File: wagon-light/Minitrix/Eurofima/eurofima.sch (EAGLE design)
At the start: 55 parts, among them IC2 78L05F, IC3 16F18324-SL, Q1 BC817-25SMD, Q2 BC817-16SMD, Q3 BC817-16SMD, Q4 BC817-16SMD, Q5 BC817-16SMD, Q6 BC817-16SMD, Q7 BC817-16SMD, Q8 BC817-16SMD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

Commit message: roco eurofima
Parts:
- removed LED17, LED18: (no value), led:LED3MM
- removed R10, R5, R6, R9: (no value), rcl:R-EU_R1206
- added Q10, Q11, Q12, Q13: BC817-16SMD, transistor-npn:BC817-16SMD
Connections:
- removed net N$8: LED5.A, R6.1
- removed net N$9: LED1.A, R3.1
- removed net PWM7: Q4.B, Q5.C
- removed net PWM8: Q6.B, Q7.C
- removed net PWM9: Q8.B, Q9.C
- net +15V: now also LED1.A, LED13.A, LED5.A, LED9.A; no longer LED18.A, R3.2, R4.2, R5.2, R6.2
- net GND: now also Q11.E, Q13.E, R3.1, R4.1
- net N$27: now also Q10.C; no longer LED17.C, R9.2
- net N$29: now also Q12.C; no longer LED18.C, R10.2
- net N$6: now also Q10.E, Q11.B, R3.2; no longer LED13.A, R5.1
- net N$7: now also Q12.E, Q13.B, R4.2; no longer LED9.A, R4.1
- net PWM1: now also Q8.B, Q9.C
- net PWM2: now also Q4.B, Q5.C
- net PWM3: now also Q6.B, Q7.C; no longer Q2.B, Q3.C
- net PWM4: now also Q2.B, Q3.C
- net PWM5: now also Q10.B, Q11.C
- net PWM6: now also Q12.B, Q13.C
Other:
- moved on the sheet: LED10, LED11, LED12, LED13, LED14, LED15, LED16, LED9, Q2, Q3, Q6, Q7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

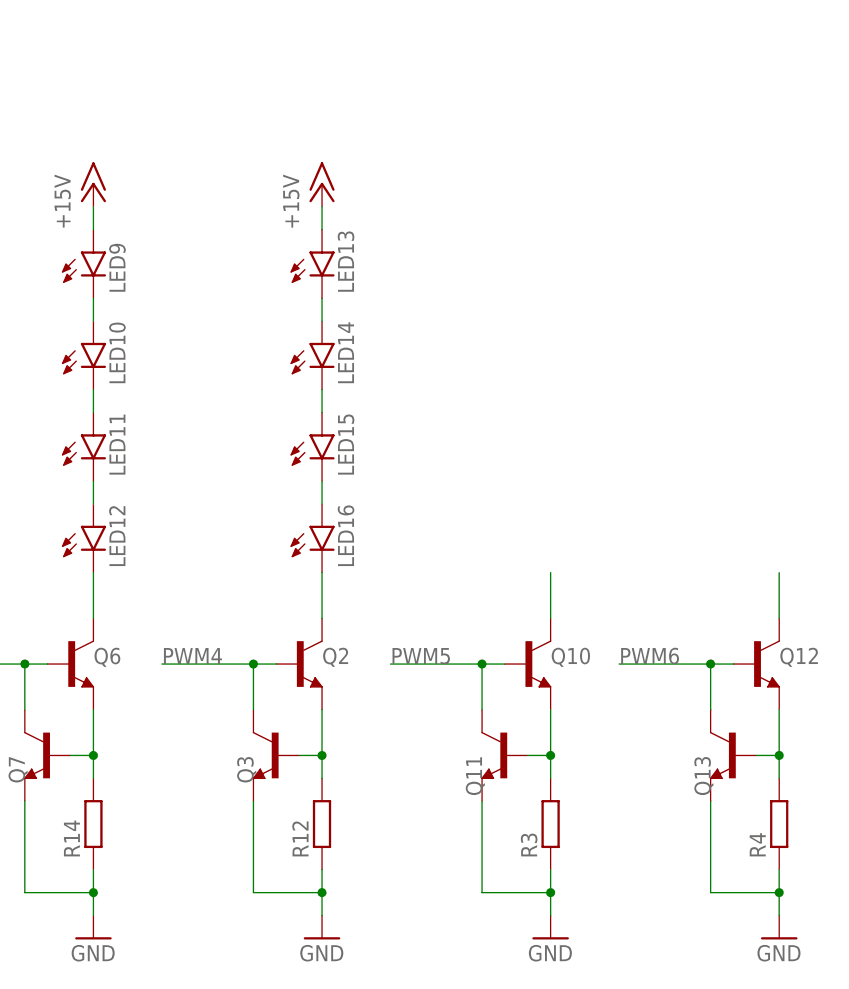
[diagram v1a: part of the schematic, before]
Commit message: legacy loc decoder
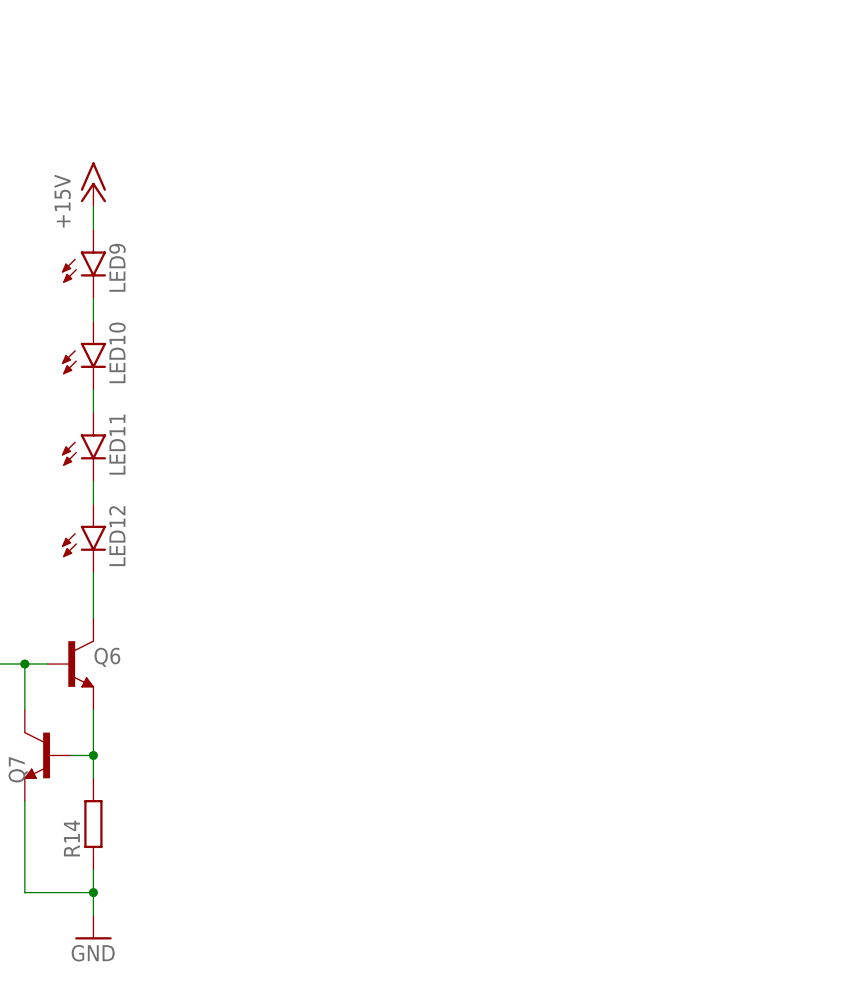
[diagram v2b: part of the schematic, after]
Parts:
- removed LED13, LED14, LED15, LED16: (no value), led:LEDKA-3528ASYC
- removed Q10, Q11, Q12, Q13, Q2, Q3: BC817-16SMD, transistor-npn:BC817-16SMD
- removed R12, R3, R4: (no value), rcl:R-EU_R1206
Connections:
- removed net N$13: LED15.C, LED16.A
- removed net N$14: LED16.C, Q2.C
- removed net N$15: LED14.C, LED15.A
- removed net N$17: Q2.E, Q3.B, R12.2
- removed net N$24: LED13.C, LED14.A
- removed net N$27: Q10.C
- removed net N$29: Q12.C
- removed net N$6: Q10.E, Q11.B, R3.2
- removed net N$7: Q12.E, Q13.B, R4.2
- net +15V: no longer LED13.A
- net GND: no longer Q11.E, Q13.E, Q3.E, R12.1, R3.1, R4.1
- net PWM4: no longer Q2.B, Q3.C
- net PWM5: no longer Q10.B, Q11.C
- net PWM6: no longer Q12.B, Q13.C

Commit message: misc
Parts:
- removed Q4, Q5, Q6, Q7, Q8, Q9: BC817-16SMD, transistor-npn:BC817-16SMD
- removed R13, R14, R15: (no value), rcl:R-EU_R1206
- added U1, U2, U3: BCR421U, BCR421U:BCR421U
- C5: device rcl:CPOL-EUA/3216-18R -> rcl:C-EUC3216
- C6, C7, C8: device rcl:CPOL-EUD/7343-31R -> rcl:C-EUC3216
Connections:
- removed net N$18: Q4.E, Q5.B, R13.2
- removed net N$25: Q6.E, Q7.B, R14.2
- removed net N$26: Q8.E, Q9.B, R15.2
- net +15V: now also C6.1, C7.1, C8.1; no longer C6.+, C7.+, C8.+
- net +5V: now also C5.1; no longer C5.+
- net GND: now also C5.2, C6.2, C7.2, C8.2, U1.GND, U2.GND, U3.GND; no longer C5.-, C6.-, C7.-, C8.-, Q5.E, Q7.E, Q9.E, R13.1, R14.1, R15.1
- net N$30: now also U1.OUT@2, U1.OUT@3, U1.OUT@5; no longer Q8.C
- net N$31: now also U3.OUT@2, U3.OUT@3, U3.OUT@5; no longer Q6.C
- net N$32: now also U2.OUT@2, U2.OUT@3, U2.OUT@5; no longer Q4.C
- net PWM1: now also U1.EN; no longer Q8.B, Q9.C
- net PWM2: now also U2.EN; no longer Q4.B, Q5.C
- net PWM3: now also U3.EN; no longer Q6.B, Q7.C
